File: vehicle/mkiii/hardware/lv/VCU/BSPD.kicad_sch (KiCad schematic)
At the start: 33 parts, among them K1 K_10A_5V, Q1 SSM3K333R,LF, Q2 SSM3K333R,LF, SW1 SW_Push_SPST_NO, SW2 SW_Push_SPST_NO, U2 SN74LVC1G08DBVR, U3 MCP6001T-I/LT, U4 SN74LVC1G02DBVR, U5 SN74LVC1G02DBVR

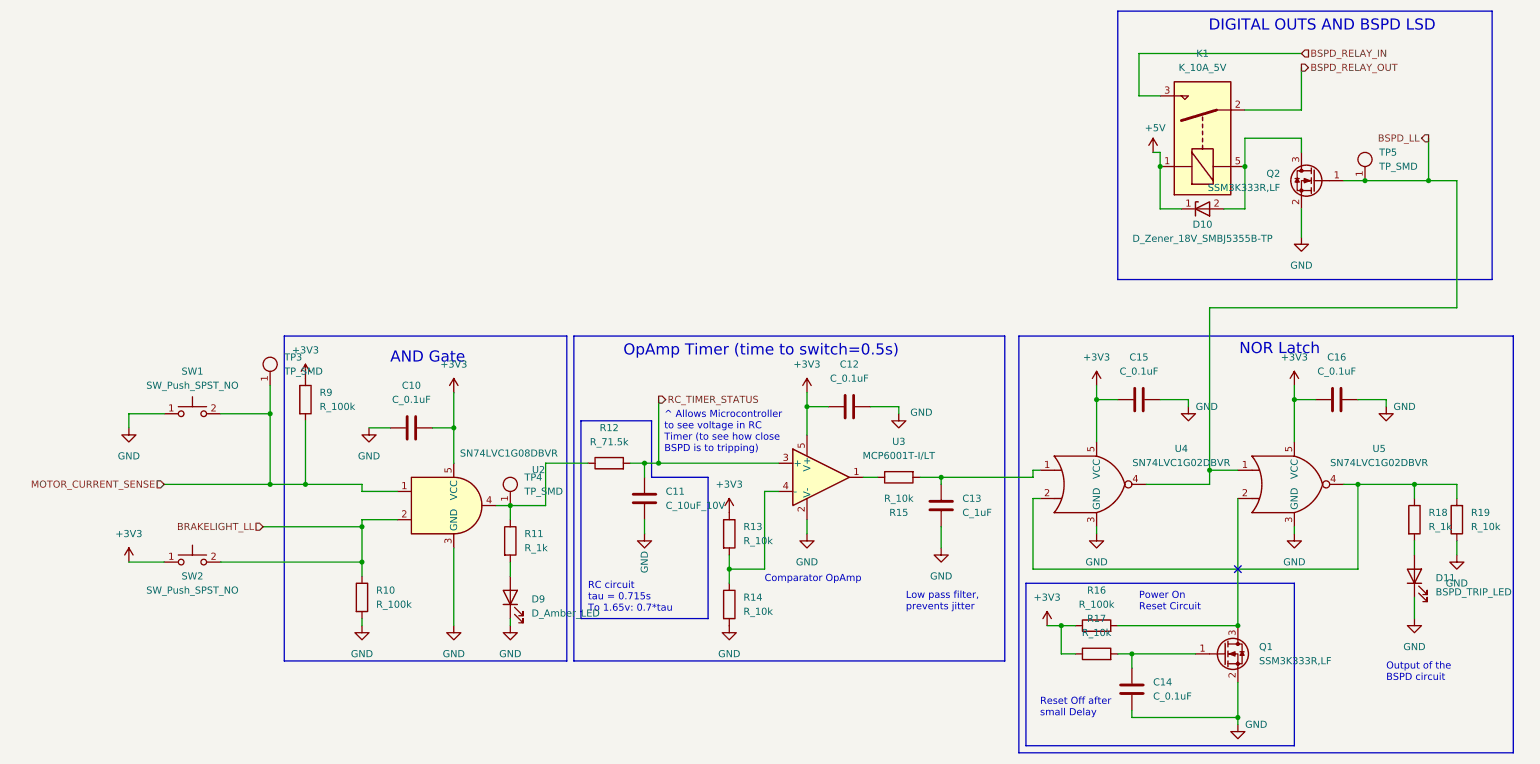
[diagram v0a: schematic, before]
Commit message: Resolved some "footprint not exist" issues
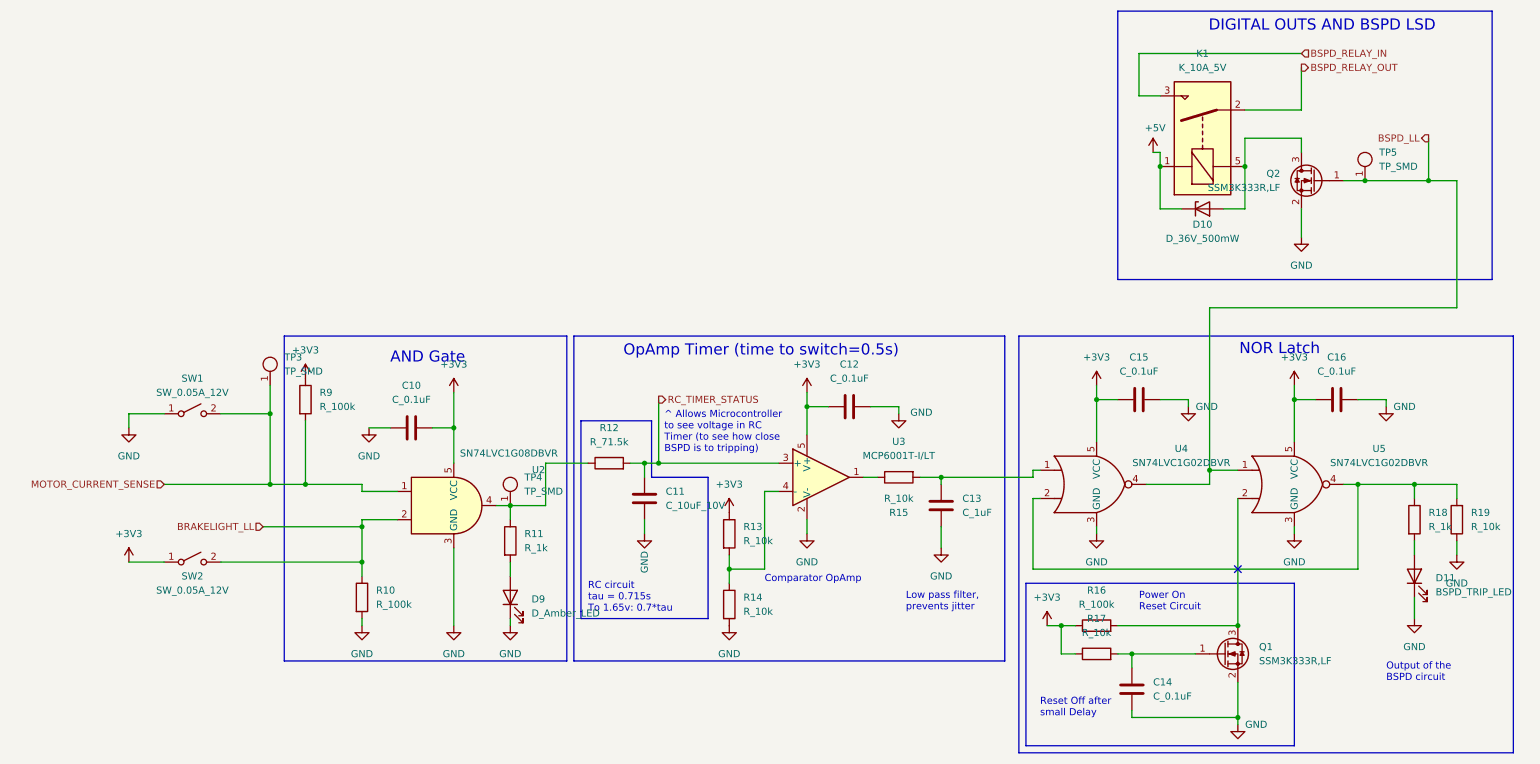
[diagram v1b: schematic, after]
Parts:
- D10: value D_Zener_18V_SMBJ5355B-TP -> D_36V_500mW; footprint OEM:DO-214AA -> OEM:D_SOD-123; symbol OEM:D_Zener_18V_SMBJ5355B-TP -> OEM:D_Zener_36V_500mW_SOD123; MPN SMBJ5355B-TP -> BZT52C36-7-F
- SW1, SW2: value SW_Push_SPST_NO -> SW_0.05A_12V; footprint OEM:SW_B3U-1000P_4.2x1.7mm -> OEM:B3U-1000P (SW_SPST_0.05A_12V_SMD - B3U-1000P); symbol OEM:SW_Push_SPST_NO -> OEM:SW_SPST_0.05A_12V_SMD_2-Pin
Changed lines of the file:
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@@
 	)
 	(symbol
-		(lib_id "OEM:D_Zener_18V_SMBJ5355B-TP")
+		(lib_id "OEM:D_Zener_36V_500mW_SOD123")
 		(at 226.06 57.15 0)
 		(unit 1)
@@
 			)
 		)
-		(property "Value" "D_Zener_18V_SMBJ5355B-TP"
+		(property "Value" "D_36V_500mW"
 			(at 226.06 62.484 0)
 			(effects
@@
 			)
 		)
-		(property "Footprint" "OEM:DO-214AA"
+		(property "Footprint" "OEM:D_SOD-123"
 			(at 226.06 57.15 0)
 			(effects
@@
 			)
 		)
-		(property "Datasheet" "https://www.mccsemi.com/pdf/Products/SMBJ5338B-SMBJ5388B(SMB).pdf"
+		(property "Datasheet" "https://www.diodes.com/assets/Datasheets/ds18004.pdf"
 			(at 226.06 57.15 0)
 			(effects
@@
 			)
 		)
-		(property "Description" "Zener diode 18V 5W 5%"
+		(property "Description" "DIODE ZENER 36V 500MW SOD123"
 			(at 226.06 57.15 0)
 			(effects
@@
 			)
 		)
-		(property "MPN" "SMBJ5355B-TP"
+		(property "MPN" "BZT52C36-7-F"
 			(at 226.06 57.15 0)
 			(effects
@@
 	)
 	(symbol
-		(lib_id "OEM:SW_Push_SPST_NO")
+		(lib_id "OEM:SW_SPST_0.05A_12V_SMD_2-Pin")
 		(at 44.45 93.98 0)
 		(unit 1)
@@
 		(fields_autoplaced yes)
 		(property "Reference" "SW1"
-			(at 44.45 86.36 0)
-			(effects
-				(font
-					(size 1.27 1.27)
-				)
-			)
-		)
-		(property "Value" "SW_Push_SPST_NO"
-			(at 44.45 88.9 0)
-			(effects
-				(font
-					(size 1.27 1.27)
-				)
-			)
-		)
-		(property "Footprint" "OEM:SW_B3U-1000P_4.2x1.7mm"
-			(at 44.45 92.71 0)
+			(at 44.45 87.63 0)
+			(effects
+				(font
+					(size 1.27 1.27)
+				)
+			)
+		)
+		(property "Value" "SW_0.05A_12V"
+			(at 44.45 90.17 0)
+			(effects
+				(font
+					(size 1.27 1.27)
+				)
+			)
+		)
+		(property "Footprint" "OEM:B3U-1000P (SW_SPST_0.05A_12V_SMD - B3U-1000P)"
+			(at 44.45 93.98 0)
 			(effects
 				(font
@@
 		)
 		(property "Datasheet" "https://omronfs.omron.com/en_US/ecb/products/pdf/en-b3u.pdf"
-			(at 44.45 92.71 0)
-			(effects
-				(font
-					(size 1.27 1.27)
-				)
-				(hide yes)
-			)
-		)
-		(property "Description" "push button SMD"
 			(at 44.45 93.98 0)
 			(effects
@@
 			)
 		)
+		(property "Description" "SWITCH TACTILE SPST-NO 0.05A 12V"
+			(at 44.45 93.98 0)
+			(effects
+				(font
+					(size 1.27 1.27)
+				)
+				(hide yes)
+			)
+		)
 		(property "MPN" "B3U-1000P"
-			(at 49.53 87.63 0)
+			(at 44.45 93.98 0)
 			(effects
 				(font
@@
 	)
 	(symbol
-		(lib_id "OEM:SW_Push_SPST_NO")
+		(lib_id "OEM:SW_SPST_0.05A_12V_SMD_2-Pin")
 		(at 44.45 120.65 0)
 		(unit 1)
@@
 			)
 		)
-		(property "Value" "SW_Push_SPST_NO"
+		(property "Value" "SW_0.05A_12V"
 			(at 44.45 125.73 0)
 			(effects
@@
 			)
 		)
-		(property "Footprint" "OEM:SW_B3U-1000P_4.2x1.7mm"
-			(at 44.45 119.38 0)
+		(property "Footprint" "OEM:B3U-1000P (SW_SPST_0.05A_12V_SMD - B3U-1000P)"
+			(at 44.45 120.65 0)
 			(effects
 				(font
@@
 		)
 		(property "Datasheet" "https://omronfs.omron.com/en_US/ecb/products/pdf/en-b3u.pdf"
-			(at 44.45 119.38 0)
-			(effects
-				(font
-					(size 1.27 1.27)
-				)
-				(hide yes)
-			)
-		)
-		(property "Description" "push button SMD"
 			(at 44.45 120.65 0)
 			(effects
@@
 			)
 		)
+		(property "Description" "SWITCH TACTILE SPST-NO 0.05A 12V"
+			(at 44.45 120.65 0)
+			(effects
+				(font
+					(size 1.27 1.27)
+				)
+				(hide yes)
+			)
+		)
 		(property "MPN" "B3U-1000P"
-			(at 49.53 114.3 0)
-			(effects
-				(font
+			(at 44.45 120.65 0)
+			(effects
+				(font

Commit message: Layout completed, review required
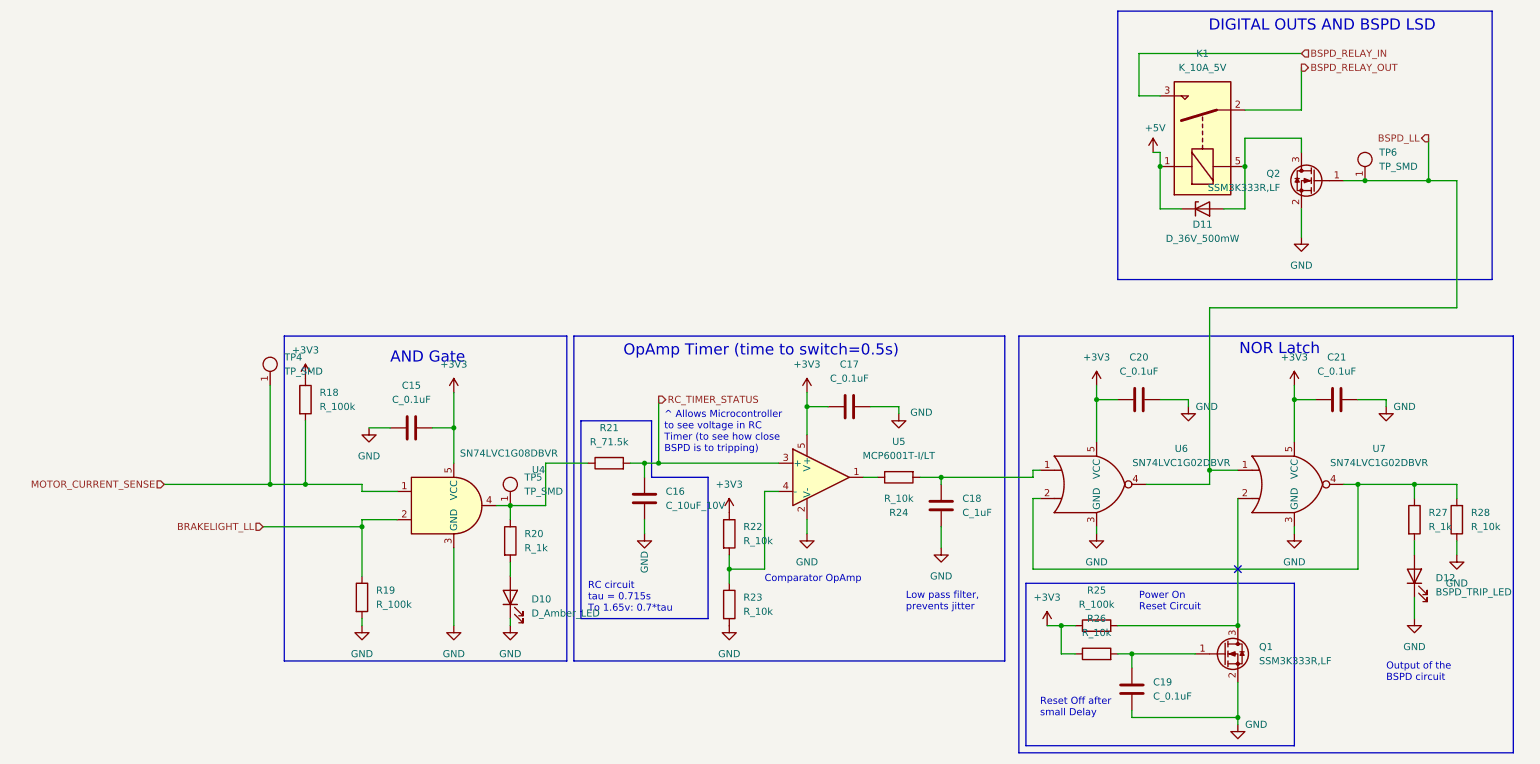
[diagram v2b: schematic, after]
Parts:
- removed SW1, SW2: SW_0.05A_12V, OEM:B3U-1000P (SW_SPST_0.05A_12V_SMD - B3U-1000P), symbol OEM:SW_SPST_0.05A_12V_SMD_2-Pin
- renumbered C10 to C15, C11 to C16, C12 to C17, C13 to C18, C14 to C19, C15 to C20, C16 to C21, D9 to D10, D10 to D11, D11 to D12, R9 to R18, R10 to R19, R11 to R20, R12 to R21, R13 to R22, R14 to R23, R15 to R24, R16 to R25, R17 to R26, R18 to R27, R19 to R28, TP3 to TP4, TP4 to TP5, TP5 to TP6, U2 to U4, U3 to U5, U4 to U6, U5 to U7
